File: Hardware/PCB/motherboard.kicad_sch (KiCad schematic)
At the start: 40 parts, among them J1 USB4105-GF-A, SW1 reset btn, U1 STM32F303VCTx, U2 USBLC6-2SC6

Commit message: added new screen and updated mcu to a more compatible one
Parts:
- removed U1: STM32F303VCTx, Package_QFP:LQFP-100_14x14mm_P0.5mm, symbol MCU_ST_STM32F3:STM32F303VCTx
- added C26, C27, C28, C31, C32: 100n, symbol Device:C
- added C29, C33: 100n, Capacitor_SMD:C_0402_1005Metric, symbol Device:C
- added C30, C34: 2u2, symbol Device:C
- added R37: 10k, symbol Device:R
- added TP22: R0, symbol Connector:TestPoint
- added TP23: R1, symbol Connector:TestPoint
- added TP24: R2, symbol Connector:TestPoint
- added TP25: R3, symbol Connector:TestPoint
- added TP26: R4, symbol Connector:TestPoint
- added TP27: R5, symbol Connector:TestPoint
- added TP28: R6, symbol Connector:TestPoint
- added TP29: R7, symbol Connector:TestPoint
- added TP30: B0, symbol Connector:TestPoint
- added TP31: B1, symbol Connector:TestPoint
- added TP32: B2, symbol Connector:TestPoint
- added TP33: B3, symbol Connector:TestPoint
- added TP34: B4, symbol Connector:TestPoint
- added TP35: B5, symbol Connector:TestPoint
- added TP36: B6, symbol Connector:TestPoint
- added TP37: B7, symbol Connector:TestPoint
- added TP38: G0, symbol Connector:TestPoint
- added TP39: G1, symbol Connector:TestPoint
- added TP40: G2, symbol Connector:TestPoint
- added TP41: G3, symbol Connector:TestPoint
- added TP42: G4, symbol Connector:TestPoint
- added TP43: G5, symbol Connector:TestPoint
- added TP44: G6, symbol Connector:TestPoint
- added TP45: G7, symbol Connector:TestPoint
- added TP46: HSYNC, symbol Connector:TestPoint
- added TP47: FSYNC, symbol Connector:TestPoint
- added TP48: SDA, symbol Connector:TestPoint
- added TP49: SCL, symbol Connector:TestPoint
- added TP50: DE, symbol Connector:TestPoint
- added TP51: PCLK, symbol Connector:TestPoint
- added TP52: STBY, symbol Connector:TestPoint
- added TP53: CS, symbol Connector:TestPoint
- added U8: STM32H743ZITx, Package_QFP:LQFP-144_20x20mm_P0.5mm, symbol MCU_ST_STM32H7:STM32H743ZITx
- C6: value 4.7u -> 4u7
- TP20: value TestPoint -> RESET
- TP21: value TestPoint -> tft-pwm
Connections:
- net +3.3V: now also C26.1, C27.1, C28.1, C29.1, C31.1, C32.1, C33.1, R37.2, U8.108 (VDD), U8.121 (VDD), U8.131 (VDD), U8.138 (BOOT0), U8.144 (VDD), U8.17 (VDD), U8.30 (VDD), U8.32 (VREF+), U8.33 (VDDA), U8.39 (VDD), U8.52 (VDD), U8.62 (VDD), U8.72 (VDD), U8.84 (VDD)
- net GND: now also C26.2, C27.2, C28.2, C29.2, C30.2, C31.2, C32.2, C33.2, C34.2, U8.102 (PA10), U8.107 (VSS), U8.120 (VSS), U8.130 (VSS), U8.16 (VSS), U8.31 (VSSA), U8.38 (VSS), U8.51 (VSS), U8.61 (VSS), U8.83 (VSS), U8.94 (VSS)
- net USB_D+: now also U8.104 (PA12)
- net USB_D-: now also U8.103 (PA11)
- net VBUS: now also U8.101 (PA9)
- net at C1.1, SW1.2: now also R37.1, U8.25 (NRST)
- net tft_rst renamed RESET
- new net: C34.1, U8.106 (VCAP)
- new net: C30.1, U8.71 (VCAP)
- new net B0: TP30.1
- new net B1: TP31.1
- new net B2: TP32.1
- new net B3: TP33.1
- new net B4: TP34.1
- new net B5: TP35.1
- new net B6: TP36.1
- new net B7: TP37.1
- new net CS: TP53.1
- new net DE: TP50.1
- new net FSYNC: TP47.1
- new net G0: TP38.1
- new net G1: TP39.1
- new net G2: TP40.1
- new net G3: TP41.1
- new net G4: TP42.1
- new net G5: TP43.1
- new net G6: TP44.1
- new net G7: TP45.1
- new net HSYNC: TP46.1
- new net PCLK: TP51.1
- new net R0: TP22.1
- new net R1: TP23.1
- new net R2: TP24.1
- new net R3: TP25.1
- new net R4: TP26.1
- new net R5: TP27.1
- new net R6: TP28.1
- new net R7: TP29.1
- new net SCL: TP49.1
- new net SDA: TP48.1
- new net STBY: TP52.1
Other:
- note added: "BLUE"
- note added: "CTRL"
- note added: "GREEN"
- note added: "RED"
- moved on the sheet: C2, C3, C4, C5, C6, J1, R13, R16, TP1, TP2, TP20, TP21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

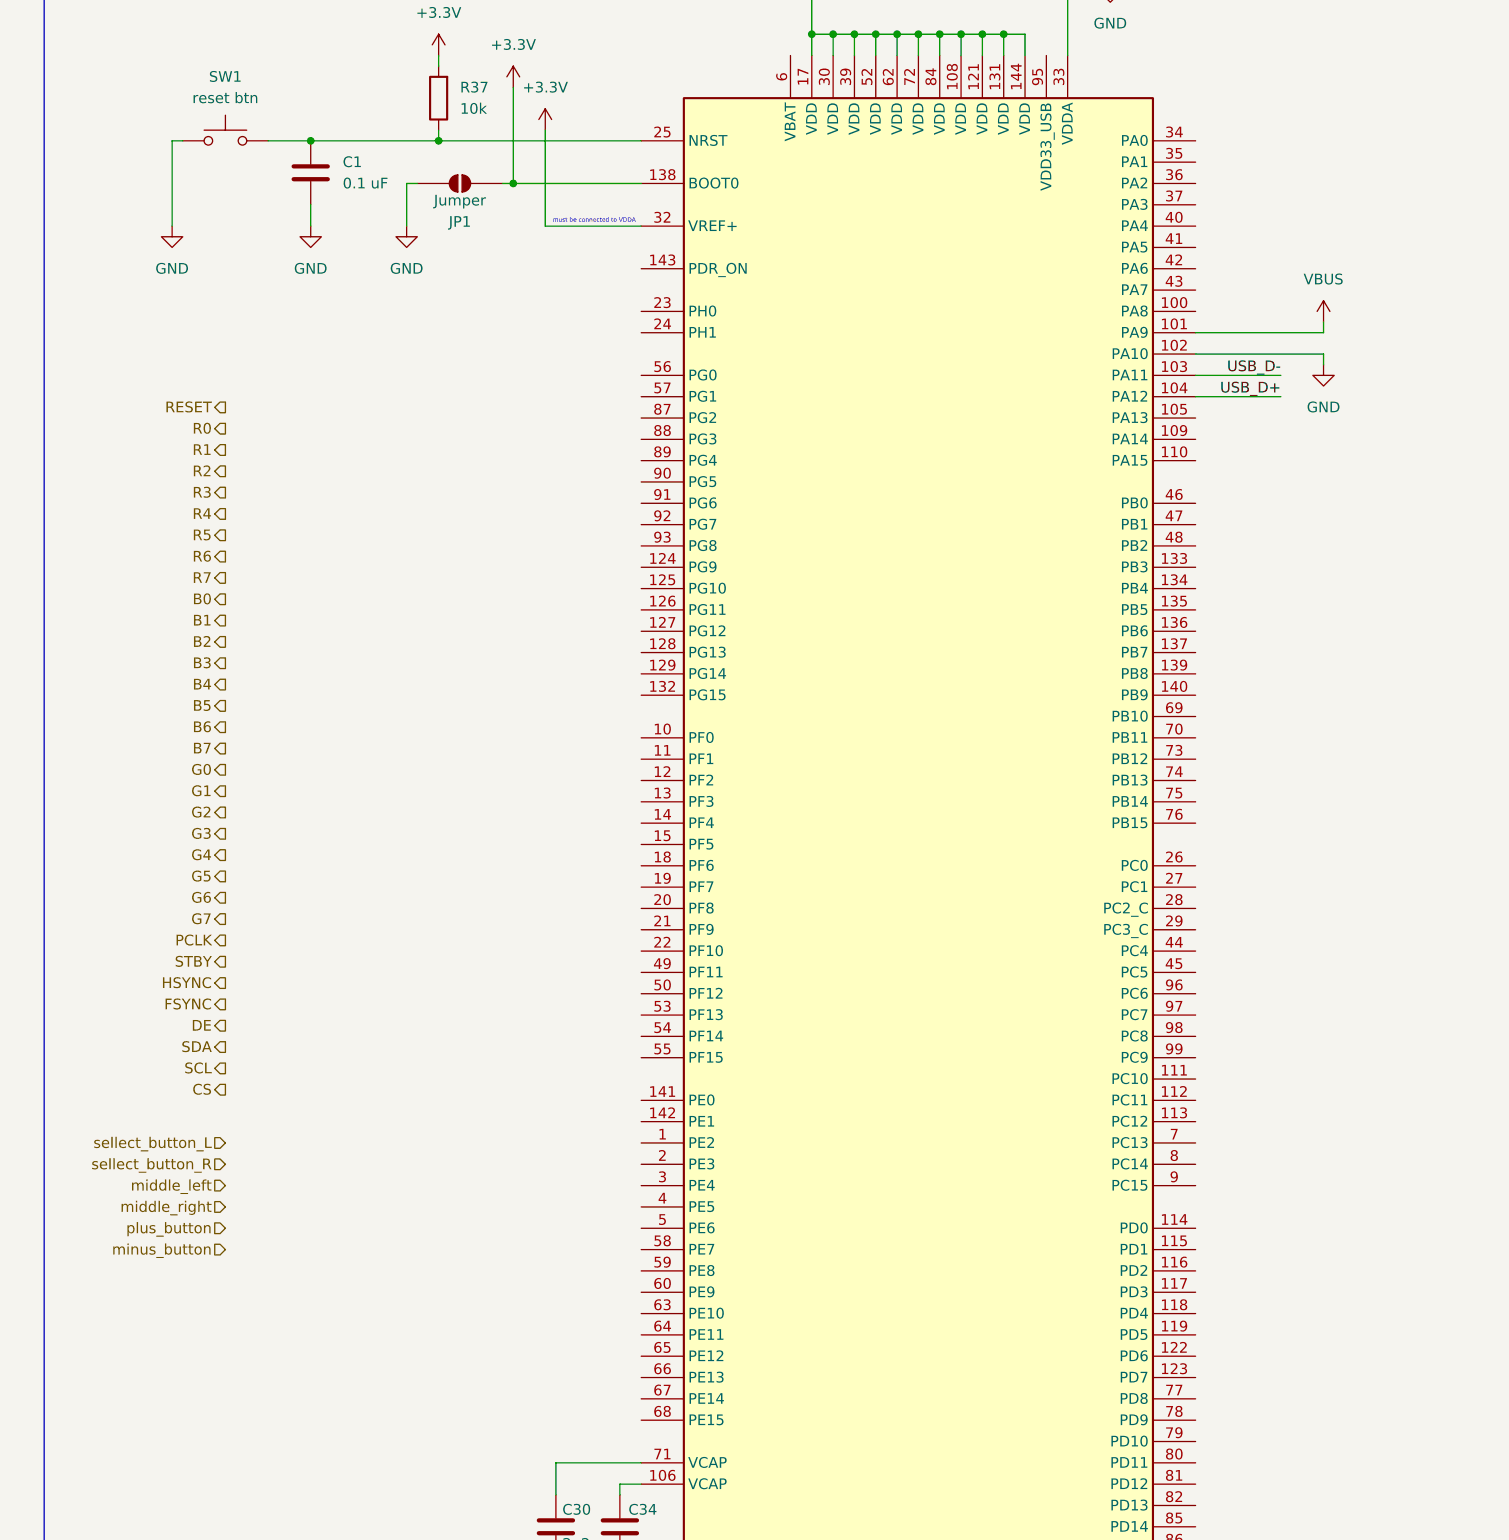
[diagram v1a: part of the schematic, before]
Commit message: connected screen
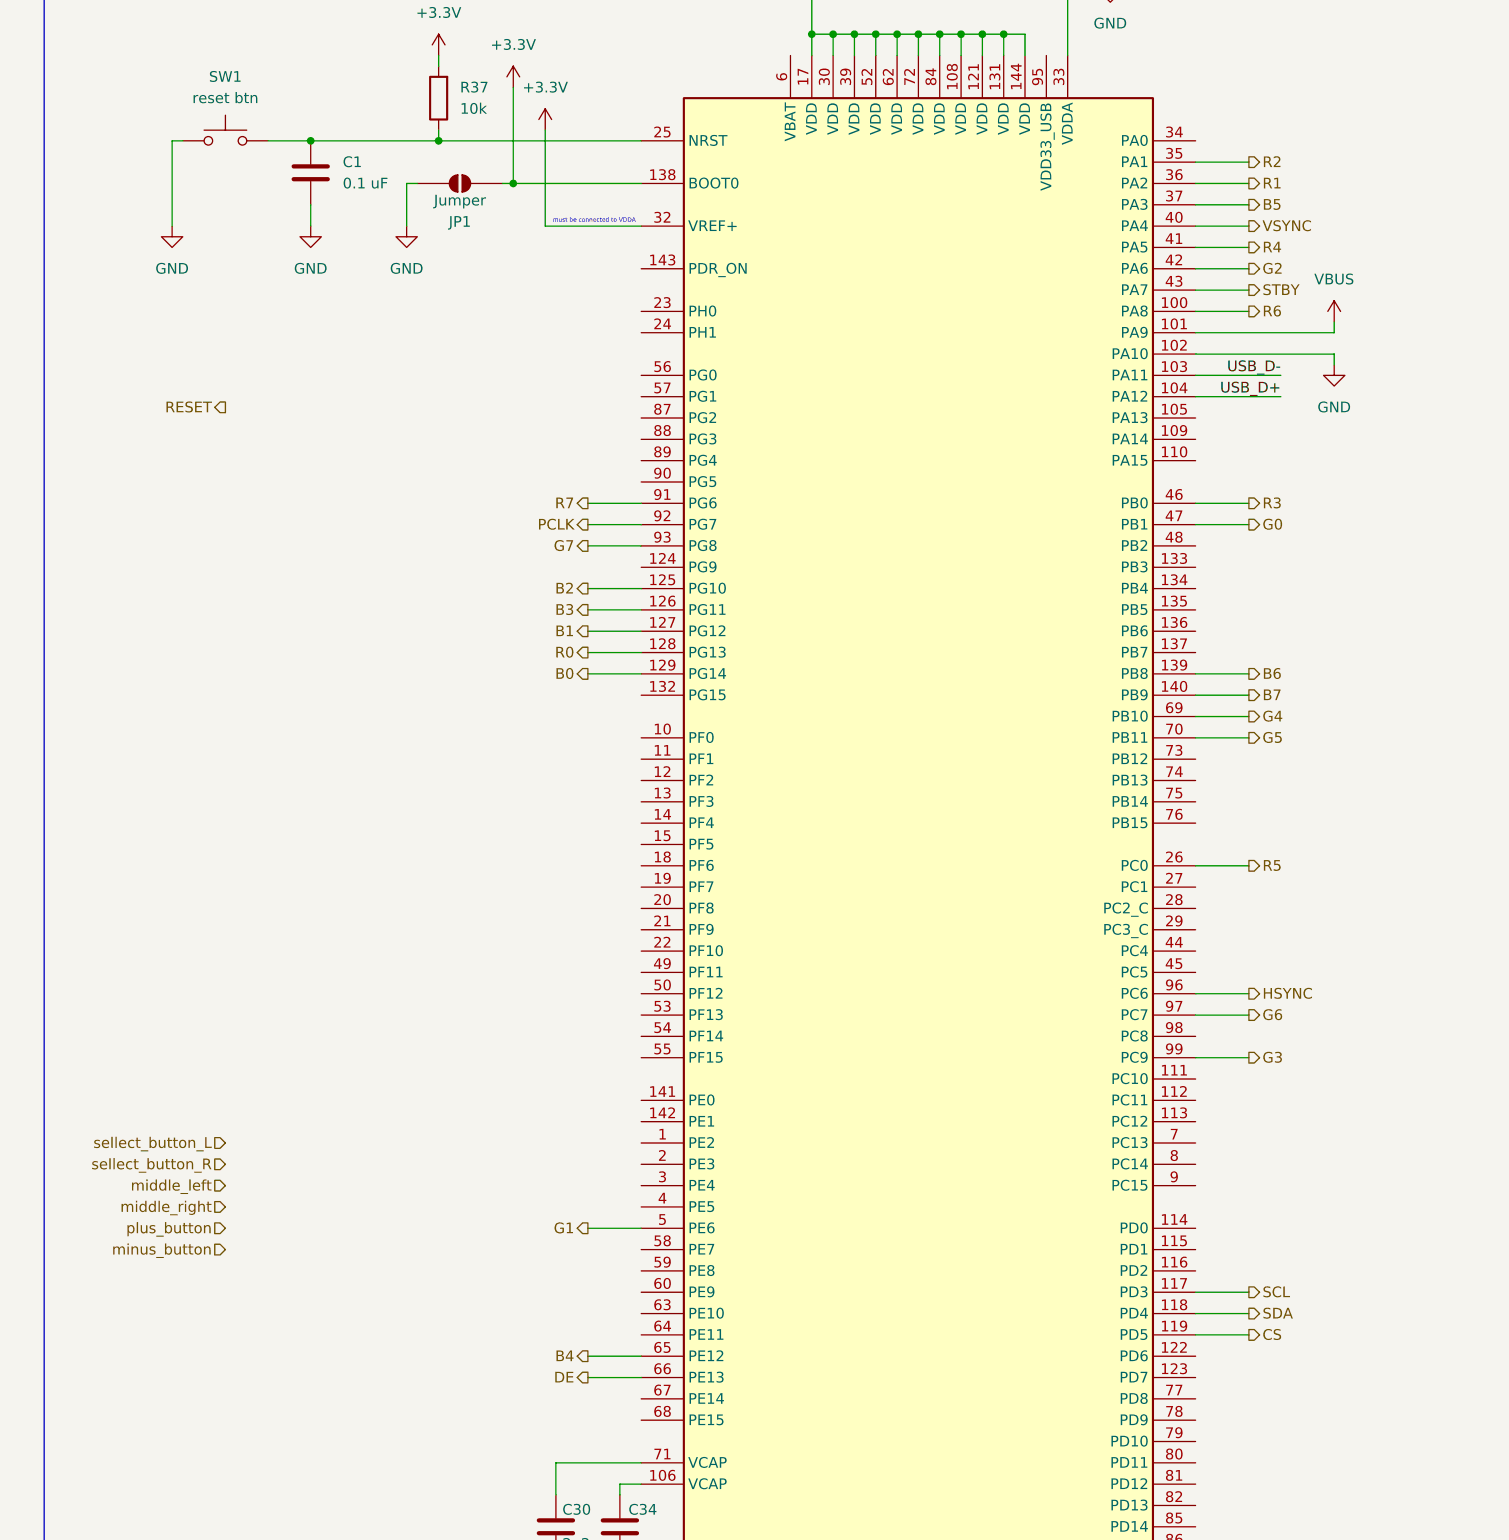
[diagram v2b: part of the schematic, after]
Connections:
- net B0: now also U8.129 (PG14)
- net B1: now also U8.127 (PG12)
- net B2: now also U8.125 (PG10)
- net B3: now also U8.126 (PG11)
- net B4: now also U8.65 (PE12)
- net B5: now also U8.37 (PA3)
- net B6: now also U8.139 (PB8)
- net B7: now also U8.140 (PB9)
- net CS: now also U8.119 (PD5)
- net DE: now also U8.66 (PE13)
- net G0: now also U8.47 (PB1)
- net G1: now also U8.5 (PE6)
- net G2: now also U8.42 (PA6)
- net G3: now also U8.99 (PC9)
- net G4: now also U8.69 (PB10)
- net G5: now also U8.70 (PB11)
- net G6: now also U8.97 (PC7)
- net G7: now also U8.93 (PG8)
- net HSYNC: now also U8.96 (PC6)
- net PCLK: now also U8.92 (PG7)
- net R0: now also U8.128 (PG13)
- net R1: now also U8.36 (PA2)
- net R2: now also U8.35 (PA1)
- net R3: now also U8.46 (PB0)
- net R4: now also U8.41 (PA5)
- net R5: now also U8.26 (PC0)
- net R6: now also U8.100 (PA8)
- net R7: now also U8.91 (PG6)
- net SCL: now also U8.117 (PD3)
- net SDA: now also U8.118 (PD4)
- net STBY: now also U8.43 (PA7)
- net VSYNC: now reaches U8.40 (PA4)

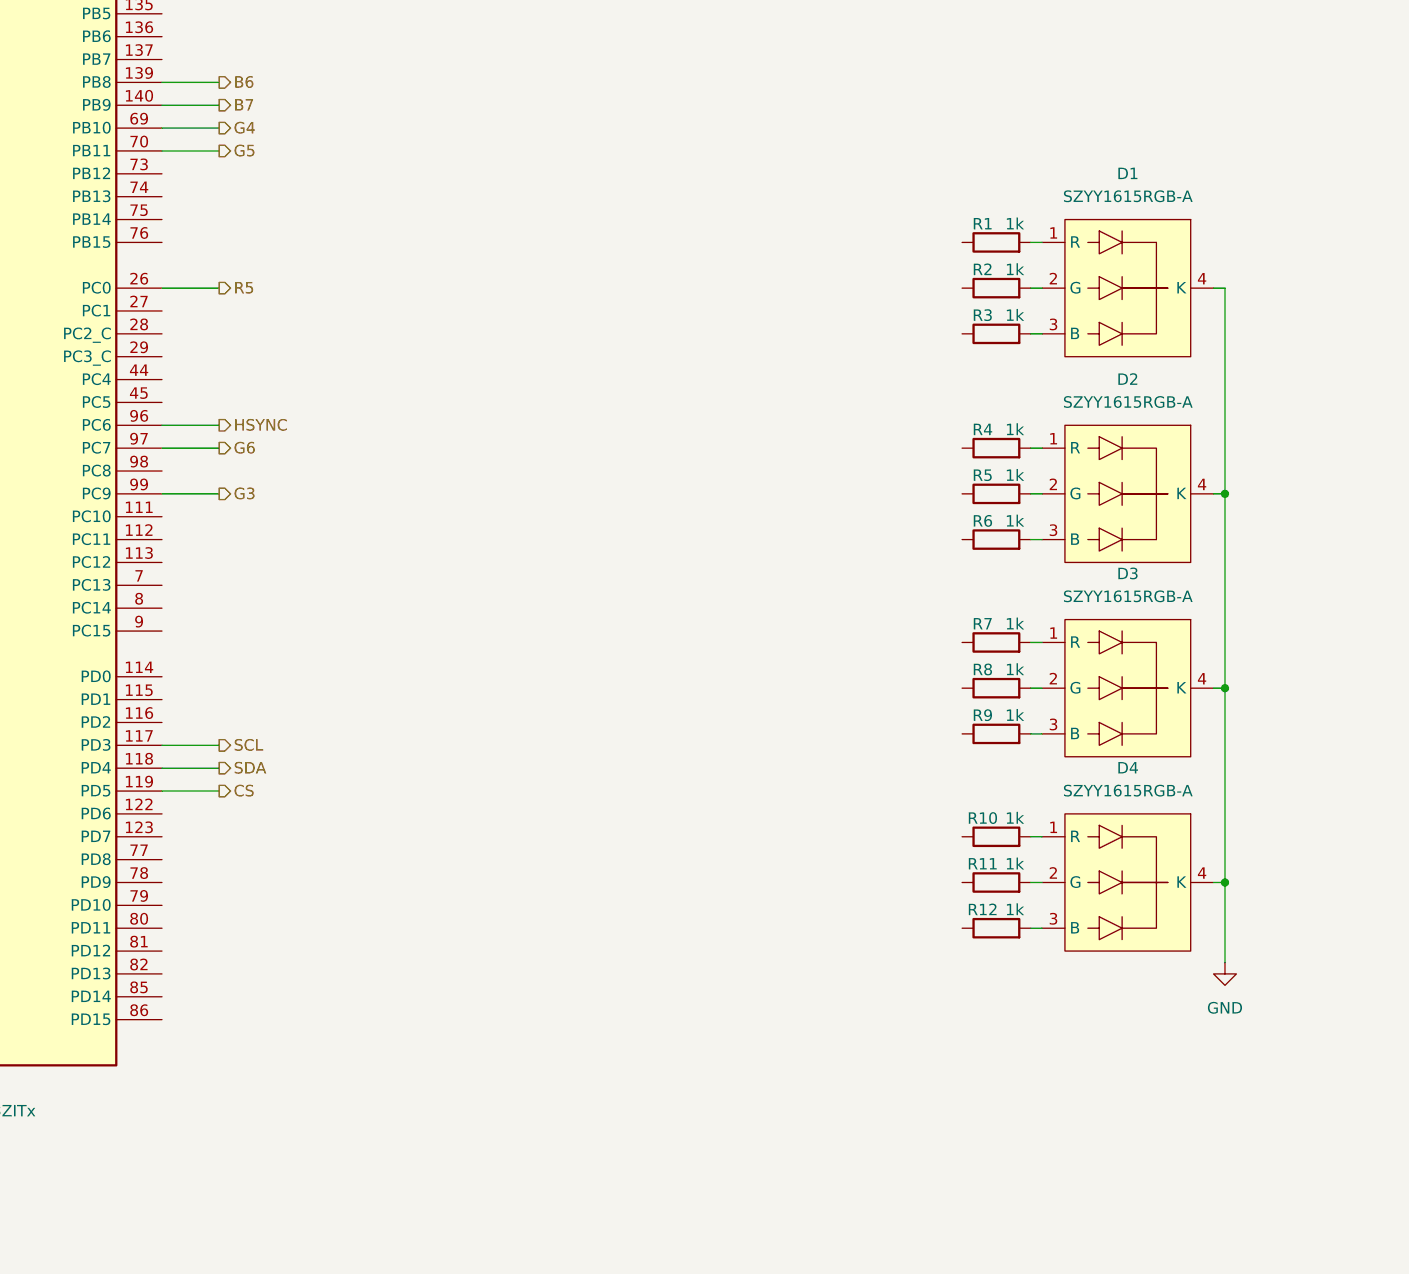
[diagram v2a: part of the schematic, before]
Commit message: fixed rgb pins again
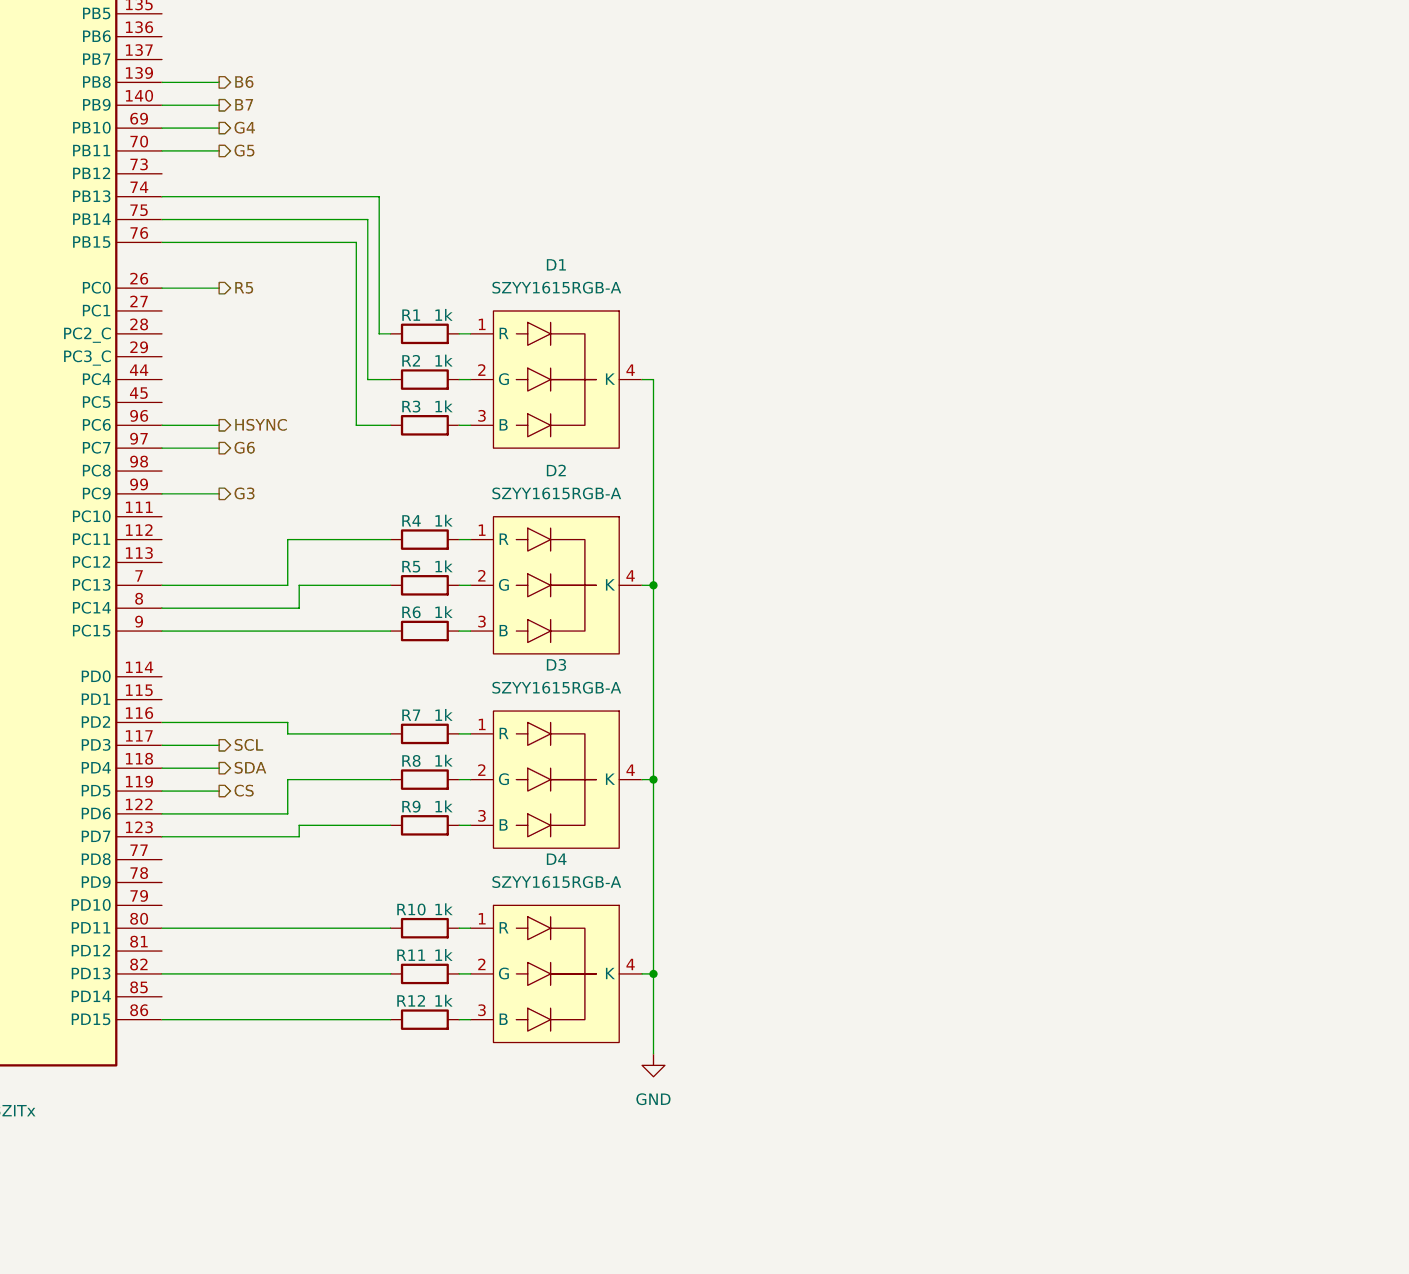
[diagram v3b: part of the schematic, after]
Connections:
- net at R1.1: now also U8.74 (PB13)
- net at R11.1: now also U8.82 (PD13)
- net at U8.116 (PD2): now also R7.1
- net at U8.122 (PD6): now also R8.1
- net at U8.123 (PD7): now also R9.1
- net at U8.7 (PC13): now also R4.1
- net at U8.75 (PB14): now also R2.1
- net at U8.76 (PB15): now also R3.1
- net at U8.8 (PC14): now also R5.1
- net at U8.80 (PD11): now also R10.1
- net at U8.86 (PD15): now also R12.1
- net at U8.9 (PC15): now also R6.1
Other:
- moved on the sheet: D1, D2, D3, D4, R1, R10, R11, R12, R2, R3, R4, R5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
